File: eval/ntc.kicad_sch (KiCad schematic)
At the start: 2 parts

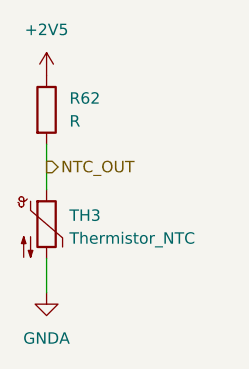
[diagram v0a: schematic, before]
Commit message: [trace] add high power trace
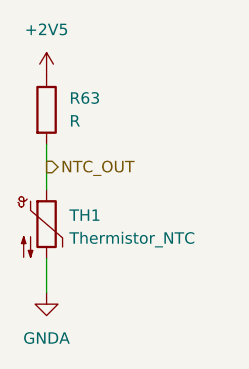
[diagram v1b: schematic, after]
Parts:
- renumbered R62 to R63, TH3 to TH1
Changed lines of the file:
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@@
 		(dnp no)
 		(fields_autoplaced yes)
-		(property "Reference" "TH3"
+		(property "Reference" "TH1"
 			(at 68.58 101.9174 0)
 			(show_name no)
@@
 				)
 				(path "/8b023652-20db-48ce-ad53-bc2d9a4e5dd4/d3253a8d-0eec-44ee-bd6d-2b47f044d90a"
-					(reference "TH3")
+					(reference "TH1")
 					(unit 1)
 				)
@@
 		(dnp no)
 		(fields_autoplaced yes)
-		(property "Reference" "#PWR0143"
+		(property "Reference" "#PWR0139"
 			(at 66.04 116.84 0)
 			(hide yes)
@@
 				)
 				(path "/8b023652-20db-48ce-ad53-bc2d9a4e5dd4/d3253a8d-0eec-44ee-bd6d-2b47f044d90a"
-					(reference "#PWR0143")
+					(reference "#PWR0139")
 					(unit 1)
 				)
@@
 		(dnp no)
 		(fields_autoplaced yes)
-		(property "Reference" "R62"
+		(property "Reference" "R63"
 			(at 68.58 88.8999 0)
 			(show_name no)
@@
 			(project "eval"
 				(path "/8b023652-20db-48ce-ad53-bc2d9a4e5dd4/16c85023-a95f-41ad-8d7f-a61a39d2b5de"
-					(reference "R62")
+					(reference "R65")
 					(unit 1)
 				)
 				(path "/8b023652-20db-48ce-ad53-bc2d9a4e5dd4/9739d650-82ca-4f3e-9870-5114b6878bac"
-					(reference "R57")
+					(reference "R64")
 					(unit 1)
 				)
 				(path "/8b023652-20db-48ce-ad53-bc2d9a4e5dd4/d3253a8d-0eec-44ee-bd6d-2b47f044d90a"
-					(reference "R62")
+					(reference "R63")
 					(unit 1)
 				)
@@
 		(dnp no)
 		(fields_autoplaced yes)
-		(property "Reference" "#PWR0142"
+		(property "Reference" "#PWR0138"
 			(at 66.04 90.17 0)
 			(hide yes)
@@
 				)
 				(path "/8b023652-20db-48ce-ad53-bc2d9a4e5dd4/9739d650-82ca-4f3e-9870-5114b6878bac"
-					(reference "#PWR0139")
+					(reference "#PWR0140")
 					(unit 1)
 				)
 				(path "/8b023652-20db-48ce-ad53-bc2d9a4e5dd4/d3253a8d-0eec-44ee-bd6d-2b47f044d90a"
-					(reference "#PWR0142")
-					(unit 1)
-				)
+					(reference "#PWR0138")
+					(unit 1)
+				)

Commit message: [layout] change latch -> trigger& software latch (plan)
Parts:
- R63, TH1: footprint (none) -> Resistor_SMD:R_0603_1608Metric
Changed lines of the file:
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@@
 			)
 		)
-		(property "Footprint" ""
+		(property "Footprint" "Resistor_SMD:R_0603_1608Metric"
 			(at 66.04 101.6 0)
 			(hide yes)
@@
 			)
 		)
-		(property "Footprint" ""
+		(property "Footprint" "Resistor_SMD:R_0603_1608Metric"
 			(at 64.262 90.17 90)
 			(hide yes)

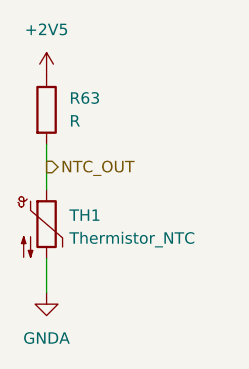
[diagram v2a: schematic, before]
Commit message: [layout&trace] layout 3 ntc sense.
Need more trace for 3 ntc, need add filter capacitor
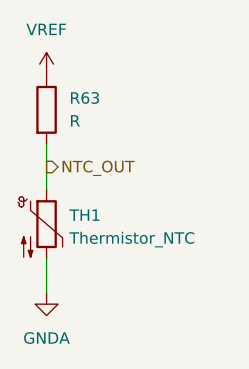
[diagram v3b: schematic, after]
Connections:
- net +2V5 renamed VREF
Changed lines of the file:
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@@
 		(dnp no)
 		(fields_autoplaced yes)
-		(property "Reference" "#PWR0138"
+		(property "Reference" "#PWR048"
 			(at 66.04 90.17 0)
 			(hide yes)
@@
 			)
 		)
-		(property "Value" "+2V5"
+		(property "Value" "VREF"
 			(at 66.04 81.28 0)
 			(show_name no)
@@
 			(project "eval"
 				(path "/8b023652-20db-48ce-ad53-bc2d9a4e5dd4/16c85023-a95f-41ad-8d7f-a61a39d2b5de"
-					(reference "#PWR0142")
+					(reference "#PWR0103")
 					(unit 1)
 				)
 				(path "/8b023652-20db-48ce-ad53-bc2d9a4e5dd4/9739d650-82ca-4f3e-9870-5114b6878bac"
-					(reference "#PWR0140")
+					(reference "#PWR072")
 					(unit 1)
 				)
 				(path "/8b023652-20db-48ce-ad53-bc2d9a4e5dd4/d3253a8d-0eec-44ee-bd6d-2b47f044d90a"
-					(reference "#PWR0138")
+					(reference "#PWR048")
 					(unit 1)
 				)
